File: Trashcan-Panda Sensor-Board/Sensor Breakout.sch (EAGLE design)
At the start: 15 parts, among them J1 BM06B-SRSS-TBT(LF)(SN), Q1 BSS215P, U1 LIS3DH, U2 VL53L1X

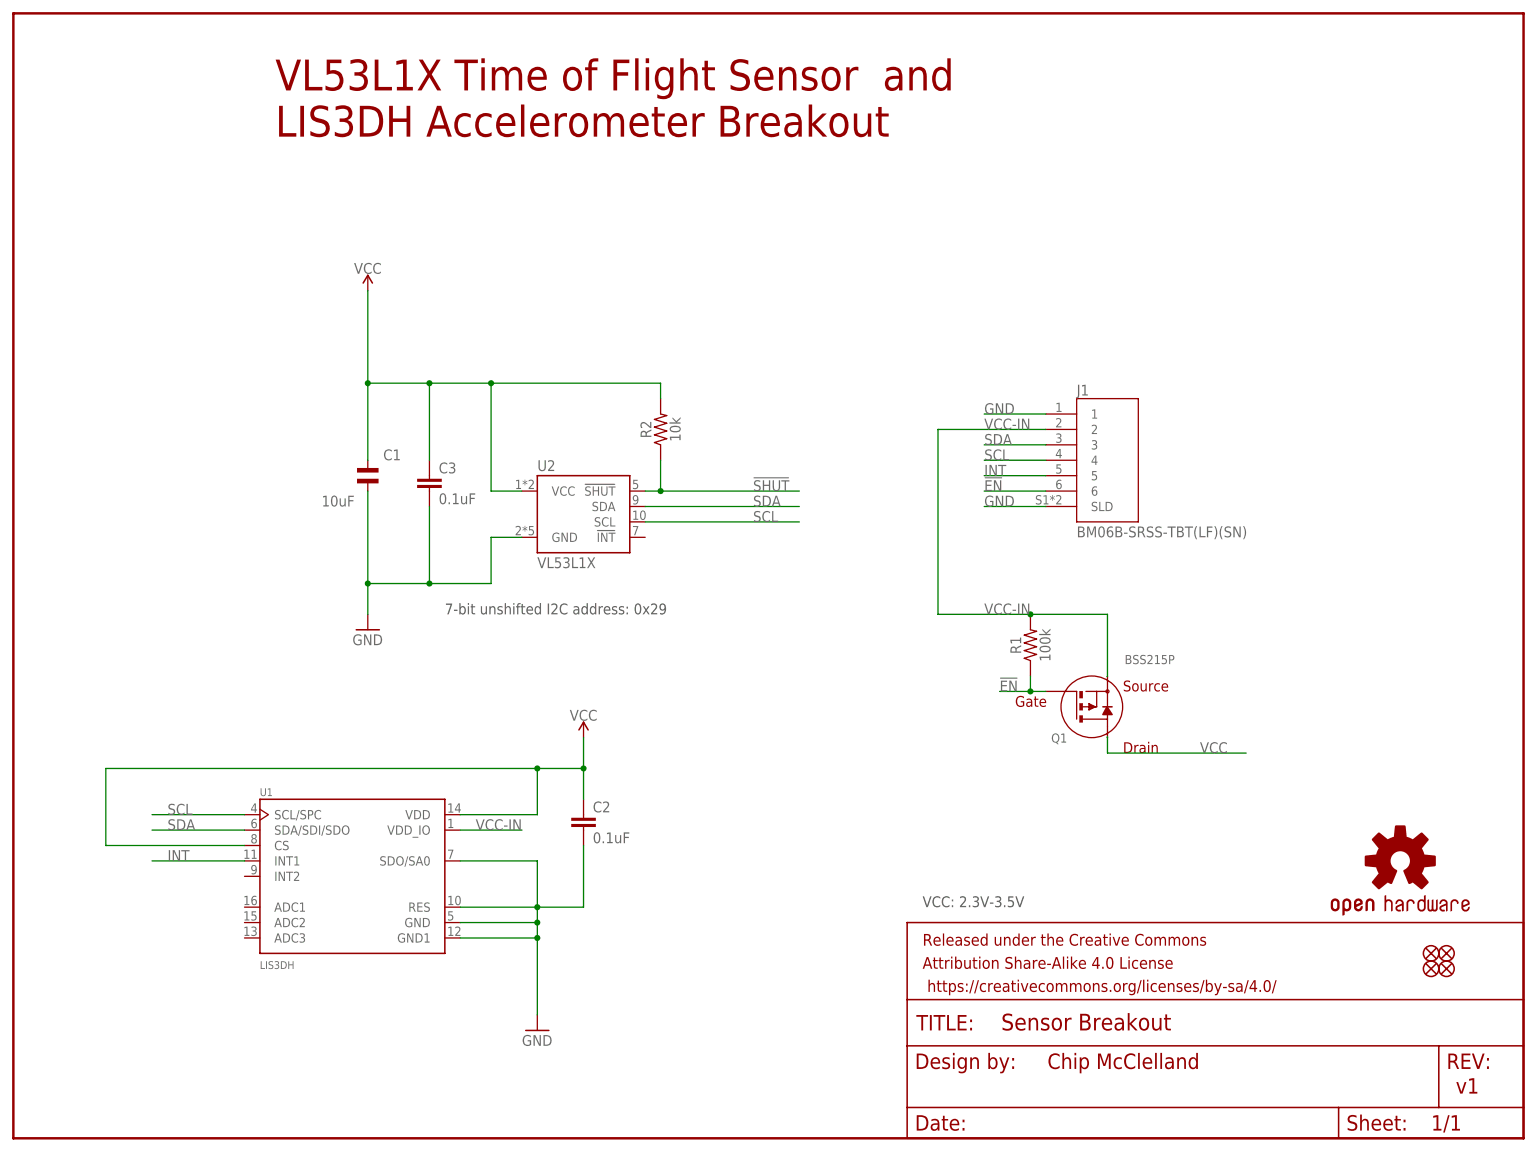
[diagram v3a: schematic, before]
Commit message: Updated for Macrofab house parts
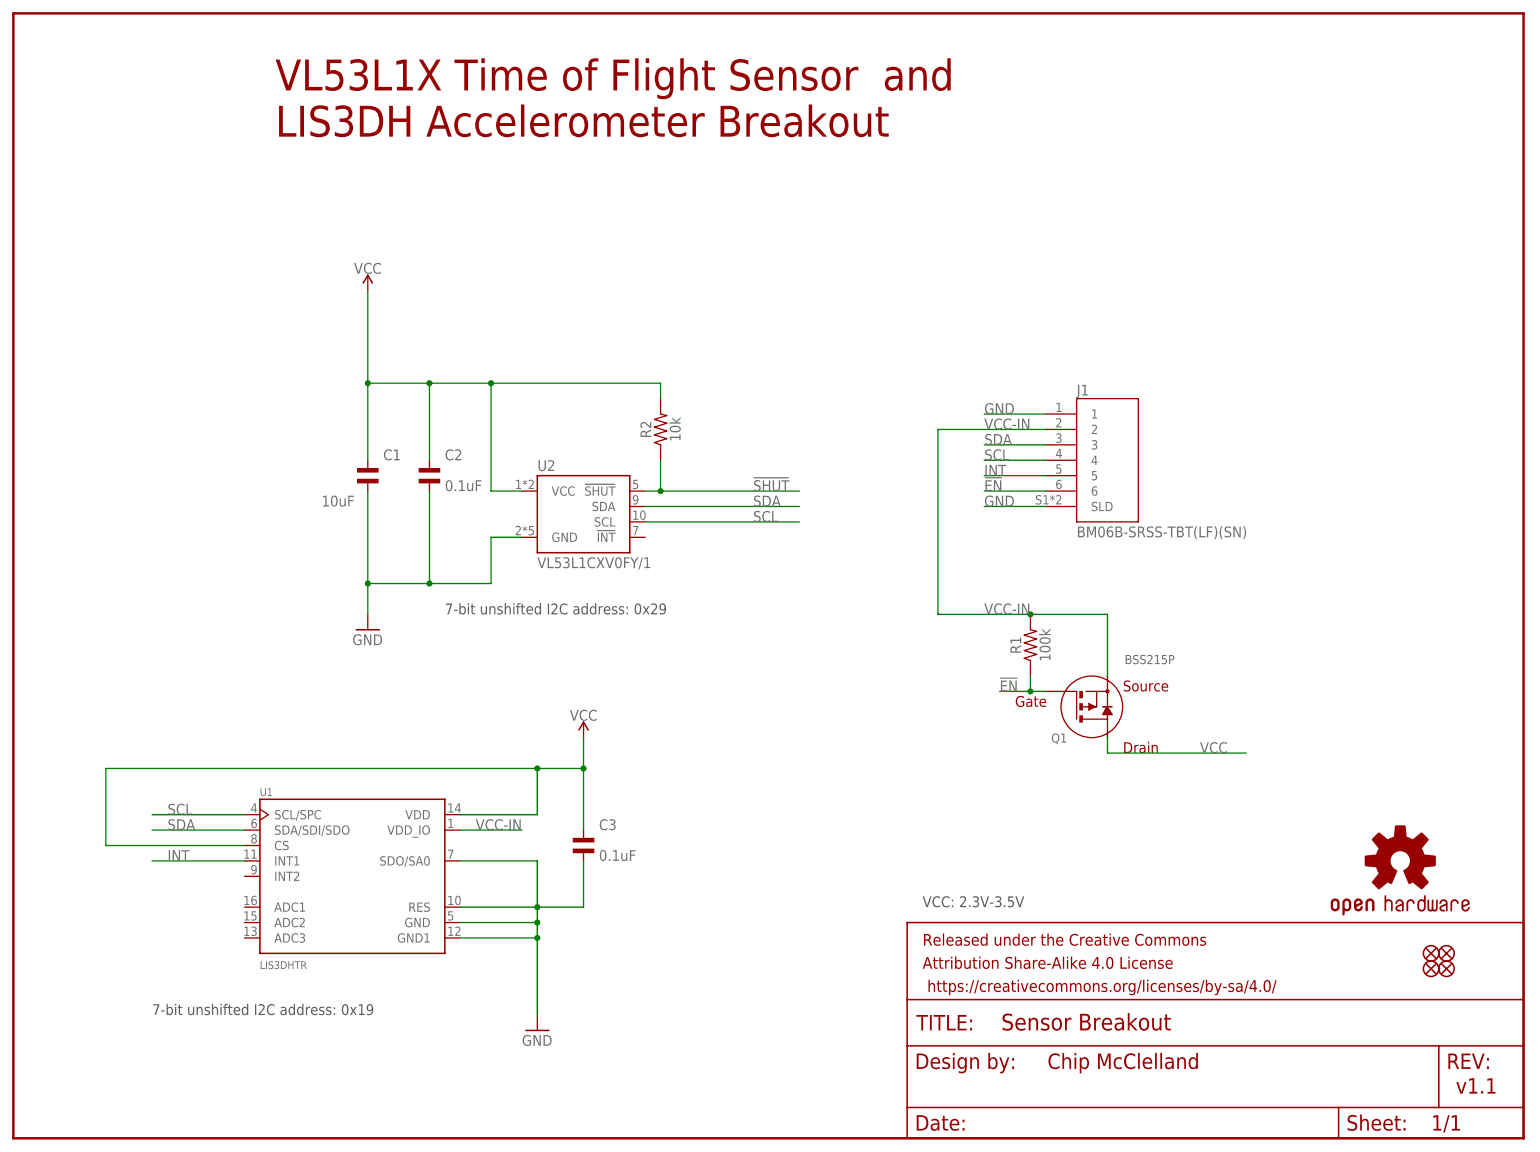
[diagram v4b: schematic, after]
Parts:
- C2, C3: device SparkFun-Capacitors:0.1UF-0603-25V-(+80/-20%) -> Custom Components:CAP-MF-0.1UF-
- FRAME1, JP1, JP2, JP5, JP6, LOGO1: POPULATE (none) -> 0
- R2: device SparkFun-Resistors:10KOHM-0603-1/10W-1% -> Custom Components:RESISTOR-MF-10K-0805
- U1: value LIS3DH -> LIS3DHTR
- U2: value VL53L1X -> VL53L1CXV0FY/1
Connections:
- net GND: now also C2.P$2, C3.P$2; no longer C2.2, C3.2
- net VCC: now also C2.P$1, C3.P$1; no longer C2.1, C3.1
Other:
- note added: "7-bit unshifted I2C address: 0x19"
- note added: "v1.1"
- note removed: "v1"
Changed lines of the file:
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@@
 </classes>
 <parts>
-<part name="JP2" library="SparkFun" deviceset="FIDUCIAL" device="UFIDUCIAL"/>
-<part name="JP6" library="SparkFun" deviceset="FIDUCIAL" device="UFIDUCIAL"/>
-<part name="FRAME1" library="SparkFun-Aesthetics" deviceset="FRAME-LETTER" device=""/>
-<part name="C3" library="SparkFun-Capacitors" deviceset="0.1UF" device="-0603-25V-(+80/-20%)" value="0.1uF"/>
-<part name="LOGO1" library="SparkFun-Aesthetics" deviceset="OSHW-LOGO" device="MINI"/>
-<part name="U2" library="SparkFun-Sensors" deviceset="VL53L1X" device="SMD" override_package3d_urn="urn:adsk.eagle:package:33496316/2" override_package_urn="urn:adsk.eagle:footprint:33496317/1" value="VL53L1X"/>
-<part name="R2" library="SparkFun-Resistors" deviceset="10KOHM" device="-0603-1/10W-1%" value="10k"/>
-<part name="JP1" library="SparkFun" deviceset="FIDUCIAL" device="UFIDUCIAL"/>
-<part name="JP5" library="SparkFun" deviceset="FIDUCIAL" device="UFIDUCIAL"/>
+<part name="JP2" library="SparkFun" deviceset="FIDUCIAL" device="UFIDUCIAL">
+<attribute name="POPULATE" value="0"/>
+</part>
+<part name="JP6" library="SparkFun" deviceset="FIDUCIAL" device="UFIDUCIAL">
+<attribute name="POPULATE" value="0"/>
+</part>
+<part name="FRAME1" library="SparkFun-Aesthetics" deviceset="FRAME-LETTER" device="">
+<attribute name="POPULATE" value="0"/>
+</part>
+<part name="LOGO1" library="SparkFun-Aesthetics" deviceset="OSHW-LOGO" device="MINI">
+<attribute name="POPULATE" value="0"/>
+</part>
+<part name="U2" library="SparkFun-Sensors" deviceset="VL53L1X" device="SMD" override_package3d_urn="urn:adsk.eagle:package:33496316/2" override_package_urn="urn:adsk.eagle:footprint:33496317/1" value="VL53L1CXV0FY/1"/>
+<part name="R2" library="Custom Components" deviceset="RESISTOR-MF-10K-" device="0805" package3d_urn="urn:adsk.eagle:package:39651/1" value="10k"/>
+<part name="JP1" library="SparkFun" deviceset="FIDUCIAL" device="UFIDUCIAL">
+<attribute name="POPULATE" value="0"/>
+</part>
+<part name="JP5" library="SparkFun" deviceset="FIDUCIAL" device="UFIDUCIAL">
+<attribute name="POPULATE" value="0"/>
+</part>
 <part name="GND2" library="SparkFun" deviceset="GND" device=""/>
 <part name="J1" library="Custom Components" deviceset="BM06B-SRSS-TBT(LF)(SN)" device=""/>
-<part name="U1" library="Custom Components" deviceset="LIS3DH" device=""/>
+<part name="U1" library="Custom Components" deviceset="LIS3DH" device="" value="LIS3DHTR"/>
 <part name="SUPPLY1" library="SparkFun-PowerSymbols" library_urn="urn:adsk.eagle:library:530" deviceset="VCC" device=""/>
 <part name="GND1" library="SparkFun" deviceset="GND" device=""/>
@@
 </part>
 <part name="Q1" library="Custom Components" deviceset="BSS215P" device=""/>
-<part name="C2" library="SparkFun-Capacitors" deviceset="0.1UF" device="-0603-25V-(+80/-20%)" value="0.1uF"/>
+<part name="C2" library="Custom Components" deviceset="CAP-MF-0.1UF-" device="" value="0.1uF"/>
+<part name="C3" library="Custom Components" deviceset="CAP-MF-0.1UF-" device="" value="0.1uF"/>
 </parts>
 <sheets>
@@
 <plain>
 <text x="170.434" y="11.43" size="2.54" layer="94" font="vector">Chip McClelland</text>
-<text x="237.744" y="7.366" size="2.54" layer="94" font="vector">v1</text>
+<text x="237.744" y="7.366" size="2.54" layer="94" font="vector">v1.1</text>
 <text x="71.12" y="86.36" size="1.778" layer="97" font="vector">7-bit unshifted I2C address: 0x29</text>
 <text x="149.86" y="38.1" size="1.778" layer="97">VCC: 2.3V-3.5V</text>
 <text x="43.18" y="165.1" size="5.08" layer="94">VL53L1X Time of Flight Sensor  and
 LIS3DH Accelerometer Breakout</text>
+<text x="22.86" y="20.32" size="1.778" layer="97" font="vector">7-bit unshifted I2C address: 0x19</text>
 </plain>
 <instances>
-<instance part="JP2" gate="G$1" x="233.68" y="30.48" smashed="yes"/>
-<instance part="JP6" gate="G$1" x="236.22" y="30.48" smashed="yes"/>
-<instance part="FRAME1" gate="G$1" x="0" y="0" smashed="yes"/>
+<instance part="JP2" gate="G$1" x="233.68" y="30.48" smashed="yes">
+<attribute name="POPULATE" x="233.68" y="30.48" size="1.778" layer="96" display="off"/>
+</instance>
+<instance part="JP6" gate="G$1" x="236.22" y="30.48" smashed="yes">
+<attribute name="POPULATE" x="236.22" y="30.48" size="1.778" layer="96" display="off"/>
+</instance>
+<instance part="FRAME1" gate="G$1" x="0" y="0" smashed="yes">
+<attribute name="POPULATE" x="0" y="0" size="1.778" layer="96" display="off"/>
+</instance>
 <instance part="FRAME1" gate="V" x="147.32" y="0" smashed="yes">
 <attribute name="LAST_DATE_TIME" x="160.02" y="1.27" size="2.54" layer="94" font="vector"/>
@@
 <attribute name="DRAWING_NAME" x="162.814" y="17.78" size="2.7432" layer="94" font="vector"/>
 </instance>
-<instance part="C3" gate="G$1" x="68.58" y="106.68" smashed="yes">
-<attribute name="NAME" x="70.104" y="109.601" size="1.778" layer="95" font="vector"/>
-<attribute name="VALUE" x="70.104" y="104.521" size="1.778" layer="96" font="vector"/>
-</instance>
-<instance part="LOGO1" gate="G$1" x="228.6" y="45.72" smashed="yes"/>
+<instance part="LOGO1" gate="G$1" x="228.6" y="45.72" smashed="yes">
+<attribute name="POPULATE" x="228.6" y="45.72" size="1.778" layer="96" display="off"/>
+</instance>
 <instance part="U2" gate="U1" x="93.98" y="101.6" smashed="yes">
 <attribute name="NAME" x="86.36" y="109.982" size="1.778" layer="95"/>
@@
 <attribute name="VALUE" x="108.204" y="116.84" size="1.778" layer="96" font="vector" rot="R90" align="top-center"/>
 </instance>
-<instance part="JP1" gate="G$1" x="236.22" y="27.94" smashed="yes"/>
-<instance part="JP5" gate="G$1" x="233.68" y="27.94" smashed="yes"/>
+<instance part="JP1" gate="G$1" x="236.22" y="27.94" smashed="yes">
+<attribute name="POPULATE" x="236.22" y="27.94" size="1.778" layer="96" display="off"/>
+</instance>
+<instance part="JP5" gate="G$1" x="233.68" y="27.94" smashed="yes">
+<attribute name="POPULATE" x="233.68" y="27.94" size="1.778" layer="96" display="off"/>
+</instance>
 <instance part="GND2" gate="1" x="58.42" y="83.82" smashed="yes">
 <attribute name="VALUE" x="55.88" y="81.28" size="1.778" layer="96"/>
@@
 <attribute name="NAME" x="171.06" y="66.72" size="1.5" layer="95" ratio="0" rot="MR180"/>
 </instance>
-<instance part="C2" gate="G$1" x="93.98" y="50.8" smashed="yes">
-<attribute name="NAME" x="95.504" y="53.721" size="1.778" layer="95" font="vector"/>
-<attribute name="VALUE" x="95.504" y="48.641" size="1.778" layer="96" font="vector"/>
+<instance part="C2" gate="G$1" x="68.58" y="109.22" smashed="yes">
+<attribute name="NAME" x="71.12" y="111.76" size="1.778" layer="95"/>
+<attribute name="VALUE" x="71.12" y="106.68" size="1.778" layer="96"/>
+</instance>
+<instance part="C3" gate="G$1" x="93.98" y="48.26" smashed="yes">
+<attribute name="NAME" x="96.52" y="50.8" size="1.778" layer="95"/>
+<attribute name="VALUE" x="96.52" y="45.72" size="1.778" layer="96"/>
 </instance>
 </instances>
@@
 <pinref part="GND2" gate="1" pin="GND"/>
 <wire x1="58.42" y1="86.36" x2="58.42" y2="91.44" width="0.1524" layer="91"/>
-<pinref part="C3" gate="G$1" pin="2"/>
 <wire x1="58.42" y1="91.44" x2="58.42" y2="106.68" width="0.1524" layer="91"/>
-<wire x1="68.58" y1="104.14" x2="68.58" y2="91.44" width="0.1524" layer="91"/>
+<wire x1="68.58" y1="106.68" x2="68.58" y2="91.44" width="0.1524" layer="91"/>
 <wire x1="68.58" y1="91.44" x2="58.42" y2="91.44" width="0.1524" layer="91"/>
 <junction x="58.42" y="91.44"/>
@@
 <junction x="68.58" y="91.44"/>
 <pinref part="C1" gate="A" pin="P$2"/>
+<pinref part="C2" gate="G$1" pin="P$2"/>
 </segment>
 <segment>
@@
 <wire x1="86.36" y1="33.02" x2="86.36" y2="20.32" width="0.1524" layer="91"/>
 <wire x1="73.66" y1="35.56" x2="86.36" y2="35.56" width="0.1524" layer="91"/>
-<pinref part="C2" gate="G$1" pin="2"/>
 <junction x="86.36" y="35.56"/>
 <pinref part="U1" gate="G$1" pin="RES"/>
@@
 <wire x1="86.36" y1="45.72" x2="86.36" y2="38.1" width="0.1524" layer="91"/>
 <wire x1="86.36" y1="38.1" x2="93.98" y2="38.1" width="0.1524" layer="91"/>
-<wire x1="93.98" y1="38.1" x2="93.98" y2="48.26" width="0.1524" layer="91"/>
+<wire x1="93.98" y1="38.1" x2="93.98" y2="45.72" width="0.1524" layer="91"/>
+<pinref part="C3" gate="G$1" pin="P$2"/>
 </segment>
 </net>
@@
 <wire x1="73.66" y1="53.34" x2="86.36" y2="53.34" width="0.1524" layer="91"/>
 <wire x1="86.36" y1="53.34" x2="86.36" y2="60.96" width="0.1524" layer="91"/>
-<pinref part="C2" gate="G$1" pin="1"/>
 <pinref part="U1" gate="G$1" pin="CS"/>
 <wire x1="38.1" y1="48.26" x2="15.24" y2="48.26" width="0.1524" layer="91"/>
@@
 <junction x="86.36" y="60.96"/>
 <wire x1="86.36" y1="60.96" x2="93.98" y2="60.96" width="0.1524" layer="91"/>
-<wire x1="93.98" y1="60.96" x2="93.98" y2="55.88" width="0.1524" layer="91"/>
+<wire x1="93.98" y1="60.96" x2="93.98" y2="50.8" width="0.1524" layer="91"/>
 <wire x1="93.98" y1="66.04" x2="93.98" y2="60.96" width="0.1524" layer="91"/>
 <junction x="93.98" y="60.96"/>
+<pinref part="C3" gate="G$1" pin="P$1"/>
 </segment>
 <segment>
@@
 <wire x1="68.58" y1="124.46" x2="58.42" y2="124.46" width="0.1524" layer="91"/>
 <wire x1="58.42" y1="111.76" x2="58.42" y2="124.46" width="0.1524" layer="91"/>
-<pinref part="C3" gate="G$1" pin="1"/>
 <wire x1="68.58" y1="111.76" x2="68.58" y2="124.46" width="0.1524" layer="91"/>
 <junction x="68.58" y="124.46"/>
@@
 <junction x="58.42" y="124.46"/>
 <pinref part="C1" gate="A" pin="P$1"/>
-</segment>
-<segment>
+<pinref part="C2" gate="G$1" pin="P$1"/>
+</segment>
+<segment>

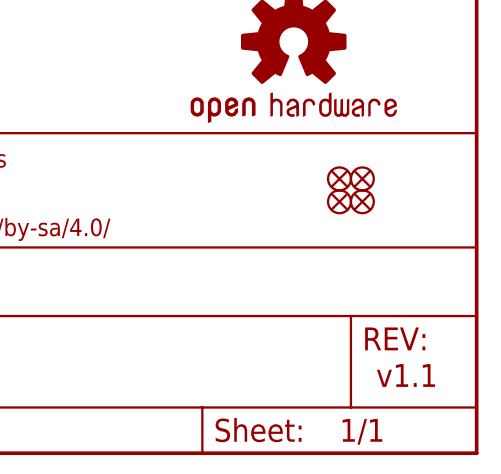
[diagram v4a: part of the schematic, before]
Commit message: Added PTC
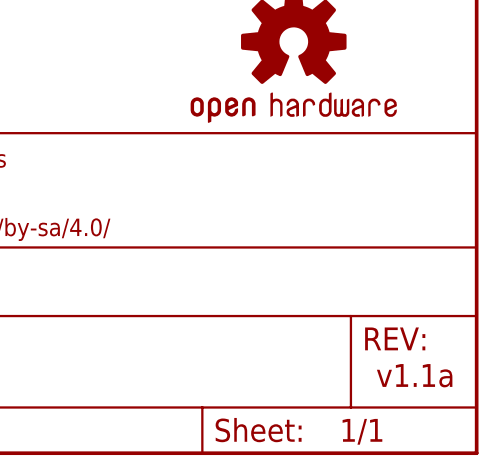
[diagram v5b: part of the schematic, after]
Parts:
- removed JP1, JP2, JP5, JP6: FIDUCIALUFIDUCIAL, SparkFun:FIDUCIALUFIDUCIAL
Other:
- note added: "v1.1a"
- note removed: "v1.1"
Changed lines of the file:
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@@
 </classes>
 <parts>
-<part name="JP2" library="SparkFun" deviceset="FIDUCIAL" device="UFIDUCIAL">
-<attribute name="POPULATE" value="0"/>
-</part>
-<part name="JP6" library="SparkFun" deviceset="FIDUCIAL" device="UFIDUCIAL">
-<attribute name="POPULATE" value="0"/>
-</part>
 <part name="FRAME1" library="SparkFun-Aesthetics" deviceset="FRAME-LETTER" device="">
 <attribute name="POPULATE" value="0"/>
@@
 <part name="U2" library="SparkFun-Sensors" deviceset="VL53L1X" device="SMD" override_package3d_urn="urn:adsk.eagle:package:33496316/2" override_package_urn="urn:adsk.eagle:footprint:33496317/1" value="VL53L1CXV0FY/1"/>
 <part name="R2" library="Custom Components" deviceset="RESISTOR-MF-10K-" device="0805" package3d_urn="urn:adsk.eagle:package:39651/1" value="10k"/>
-<part name="JP1" library="SparkFun" deviceset="FIDUCIAL" device="UFIDUCIAL">
-<attribute name="POPULATE" value="0"/>
-</part>
-<part name="JP5" library="SparkFun" deviceset="FIDUCIAL" device="UFIDUCIAL">
-<attribute name="POPULATE" value="0"/>
-</part>
 <part name="GND2" library="SparkFun" deviceset="GND" device=""/>
 <part name="J1" library="Custom Components" deviceset="BM06B-SRSS-TBT(LF)(SN)" device=""/>
@@
 <plain>
 <text x="170.434" y="11.43" size="2.54" layer="94" font="vector">Chip McClelland</text>
-<text x="237.744" y="7.366" size="2.54" layer="94" font="vector">v1.1</text>
+<text x="237.744" y="7.366" size="2.54" layer="94" font="vector">v1.1a</text>
 <text x="71.12" y="86.36" size="1.778" layer="97" font="vector">7-bit unshifted I2C address: 0x29</text>
 <text x="149.86" y="38.1" size="1.778" layer="97">VCC: 2.3V-3.5V</text>
@@
 </plain>
 <instances>
-<instance part="JP2" gate="G$1" x="233.68" y="30.48" smashed="yes">
-<attribute name="POPULATE" x="233.68" y="30.48" size="1.778" layer="96" display="off"/>
-</instance>
-<instance part="JP6" gate="G$1" x="236.22" y="30.48" smashed="yes">
-<attribute name="POPULATE" x="236.22" y="30.48" size="1.778" layer="96" display="off"/>
-</instance>
 <instance part="FRAME1" gate="G$1" x="0" y="0" smashed="yes">
 <attribute name="POPULATE" x="0" y="0" size="1.778" layer="96" display="off"/>
@@
 <attribute name="VALUE" x="108.204" y="116.84" size="1.778" layer="96" font="vector" rot="R90" align="top-center"/>
 </instance>
-<instance part="JP1" gate="G$1" x="236.22" y="27.94" smashed="yes">
-<attribute name="POPULATE" x="236.22" y="27.94" size="1.778" layer="96" display="off"/>
-</instance>
-<instance part="JP5" gate="G$1" x="233.68" y="27.94" smashed="yes">
-<attribute name="POPULATE" x="233.68" y="27.94" size="1.778" layer="96" display="off"/>
-</instance>
 <instance part="GND2" gate="1" x="58.42" y="83.82" smashed="yes">
